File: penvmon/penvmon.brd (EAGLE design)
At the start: 160 x 100 mm, 20 parts, among them IC2 7805TV, U1 ZC563900

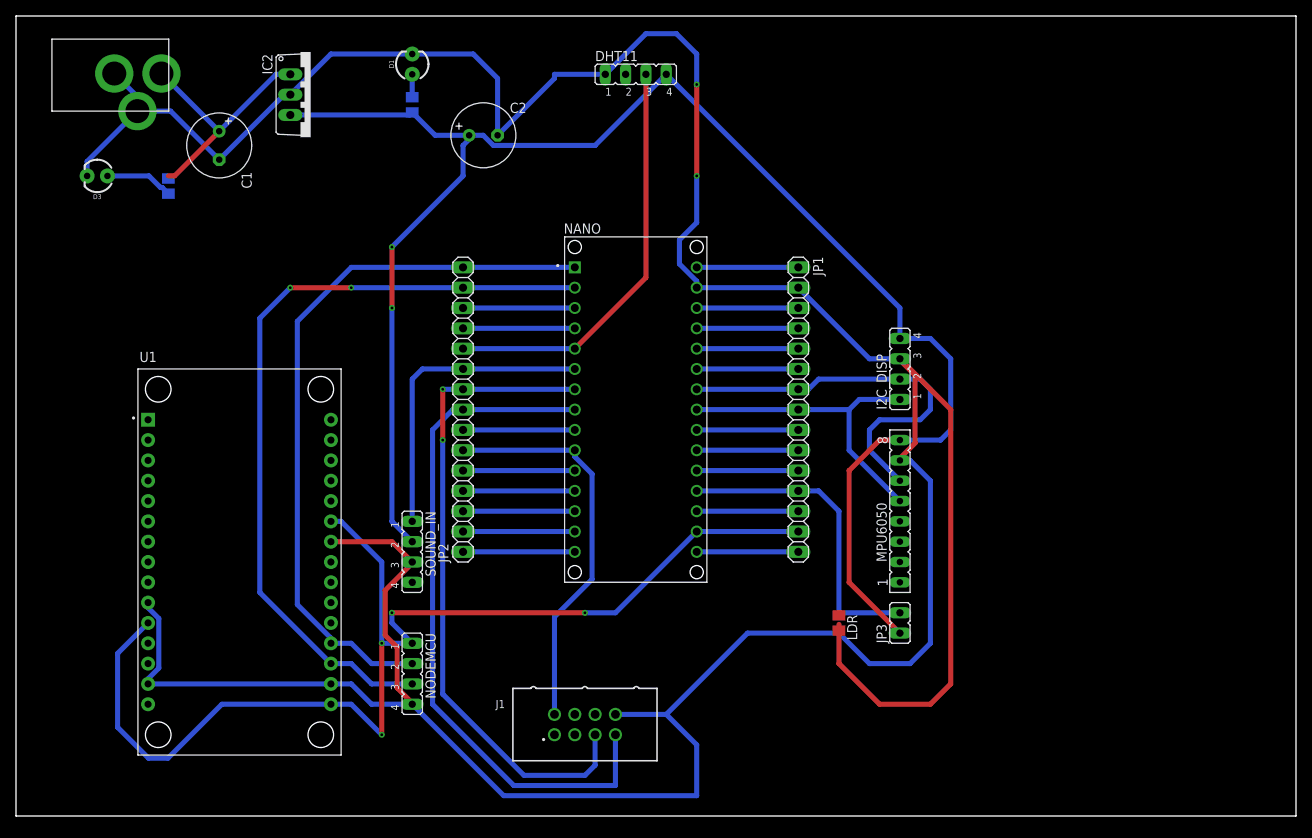
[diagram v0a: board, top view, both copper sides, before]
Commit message: changed Placement- routing and check needed
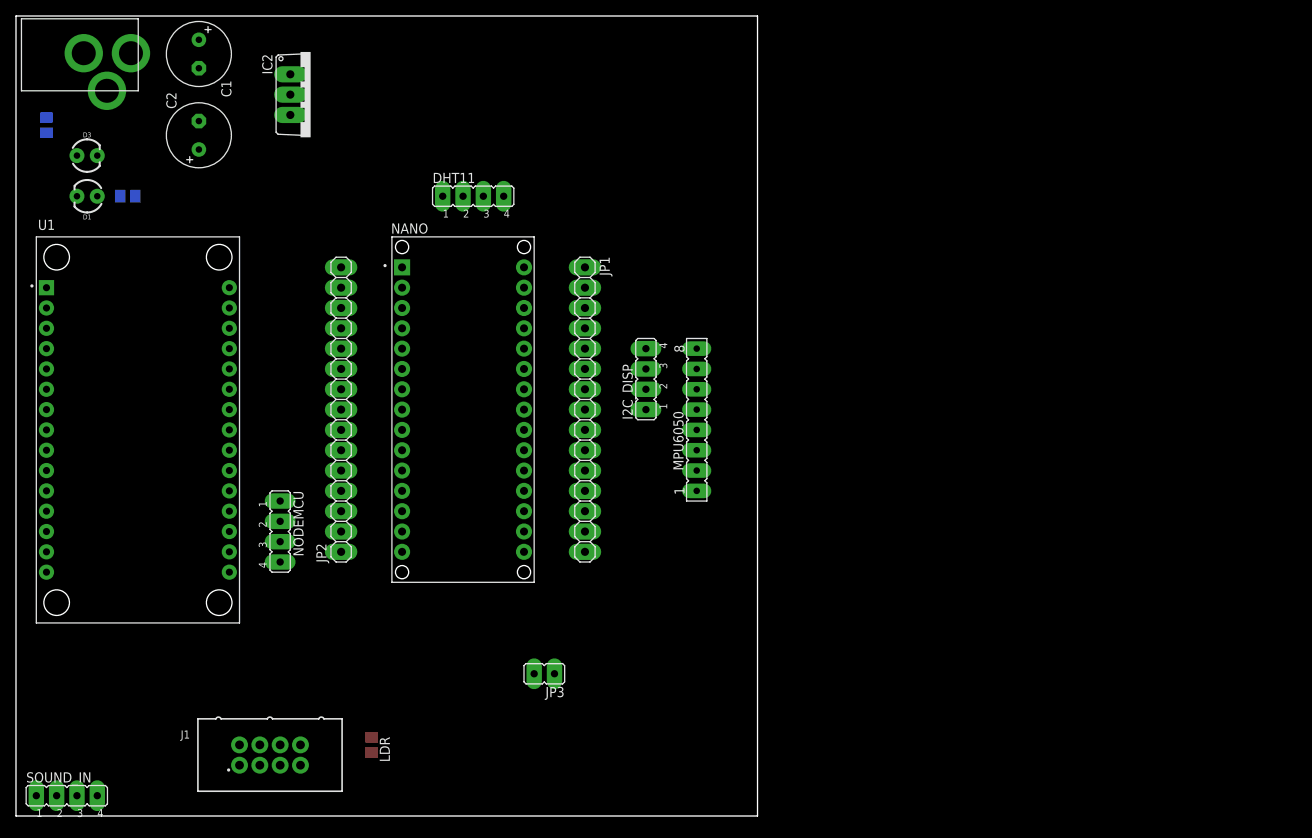
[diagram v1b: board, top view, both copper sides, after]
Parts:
- moved LDR 60.4 mm to (44.5, 8.89)
- moved SOUND_IN 52.9 mm to (6.35, 2.54), turned to 0 degrees
- moved JP3 44.9 mm to (66.0, 17.8), turned to 90 degrees
- moved D1 43.9 mm to (8.89, 77.5), turned to 180 degrees
- moved J1 39.6 mm to (31.8, 7.62)
- moved R1 37.4 mm to (14.0, 77.5), turned to 0 degrees
- moved C2 35.6 mm to (22.9, 85.1), turned to 90 degrees
- moved I2C_DISP 31.8 mm to (78.7, 54.6)
- moved MPU6050 27.9 mm to (85.1, 49.5)
- moved JP1 26.7 mm to (71.1, 50.8)
- moved DHT11 25.4 mm to (57.1, 77.5)
- moved NODEMCU 24.3 mm to (33.0, 35.6)
- moved NANO 21.6 mm to (55.9, 50.8)
- moved U1 20.8 mm to (15.2, 48.3)
- moved R11 17.0 mm to (3.81, 86.4)
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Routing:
- net GND: track 449.7 -> 0.00 mm, vias 2 -> 0
- net 5V: track 207.7 -> 0.00 mm, vias 2 -> 0
- net 3V3: track 147.3 -> 0.00 mm, vias 4 -> 0
- net RXNANO: track 99.0 -> 0.00 mm, vias 2 -> 0
- net TXNANO: track 90.7 -> 0.00 mm
- net OK: track 86.5 -> 0.00 mm
- net LEFT: track 82.2 -> 0.00 mm, vias 2 -> 0
- net DHT: track 51.9 -> 0.00 mm
- net RIGHT: track 49.8 -> 0.00 mm
- net SCL: track 49.4 -> 0.00 mm
- net SDA: track 40.0 -> 0.00 mm
- net SOUND_D0: track 39.9 -> 0.00 mm
- net LDR_SIG: track 39.2 -> 0.00 mm
- net 9_IN: track 30.7 -> 0.00 mm
- net RESET_1: track 14.0 -> 0.00 mm
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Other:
- board size 160 x 100 mm -> 92.7 x 100 mm

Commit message: vibha_layout_done
kindly check the layout once
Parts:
- removed JP3: (no value), jumper:JP1
- removed LDR: 10k, adafruit:M0805
- moved J1 25.5 mm to (57.3, 7.49)
- moved SOUND_IN 5.63 mm to (9.03, 7.49)
- moved DHT11 2.66 mm to (56.0, 79.9), turned to 180 degrees
- moved NODEMCU 1.42 mm to (32.2, 36.7)
- moved C2 1.42 mm to (24.3, 85.0)
- moved I2C_DISP 1.42 mm to (80.1, 54.5)
- moved MPU6050 1.42 mm to (86.5, 49.4)
- moved C1 1.42 mm to (24.3, 95.1)
- moved IC2 1.42 mm to (38.2, 90.0)
- moved JP1 1.42 mm to (72.5, 50.7)
- moved JP2 1.42 mm to (42.0, 50.7)
- moved NANO 1.42 mm to (57.3, 50.7)
- moved U$3 1.42 mm to (6.49, 95.1)
- moved R11 1.42 mm to (5.22, 86.2)
- moved D1 1.42 mm to (10.3, 77.3)
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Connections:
- removed net DOWN: JP2.7, NANO.9
- removed net LDR_SIG: JP1.12, JP3.2, LDR.1, NANO.19
- new net 12: JP1.12, NANO.19
- net 5V: no longer JP3.1
- net BACK: now also J1.4, JP2.7, NANO.9; no longer J1.6
- net DOWN(NA): now also J1.7; no longer J1.4
- net GND: no longer LDR.2
- net OK: now also J1.6; no longer J1.7
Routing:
- net GND: track 0.00 -> 360.2 mm
- net 5V: track 0.00 -> 184.0 mm, vias 0 -> 4
- net 3V3: track 0.00 -> 159.5 mm, vias 0 -> 7
- net SOUND_D0: track 0.00 -> 143.5 mm, vias 0 -> 6
- net LEFT: track 0.00 -> 84.3 mm, vias 0 -> 2
- net OK: track 0.00 -> 54.7 mm
- net BACK: track 0.00 -> 51.1 mm
- net RXNANO: track 0.00 -> 49.8 mm
- net TXNANO: track 0.00 -> 49.8 mm
- net RIGHT: track 0.00 -> 46.8 mm
- net 9_IN: track 0.00 -> 45.6 mm
- net DHT: track 0.00 -> 32.8 mm
- net SDA: track 0.00 -> 21.6 mm
- net SCL: track 0.00 -> 21.6 mm
- net VIN: track 0.00 -> 7.62 mm
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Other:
- board size 92.7 x 100 mm -> 91.9 x 100 mm

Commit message: just_a_little_correction_vibha_project
all the sensors are added and designed
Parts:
- added SOIL_MOI: (no value), jumper:JP4
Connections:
- removed net A7: JP1.5, NANO.26
- new net SOIL_A0: JP1.5, NANO.26, SOIL_MOI.4
- new net SOIL_D0: SOIL_MOI.3
- net 5V: now also SOIL_MOI.1
- net GND: now also SOIL_MOI.2
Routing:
- net GND: track 360.2 -> 407.9 mm
- net SOIL_A0: track 0.00 -> 32.8 mm, vias 0 -> 2
- net 5V: track 184.0 -> 213.4 mm
- net A7: track 7.62 -> 0.00 mm
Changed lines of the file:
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@@
 <attribute name="VALUE" x="89.4207" y="39.243" size="1.27" layer="27" ratio="10" rot="R90"/>
+</element>
+<element name="SOIL_MOI" library="jumper" library_urn="urn:adsk.eagle:library:252" package="JP4" package3d_urn="urn:adsk.eagle:package:15463/1" value="" x="85.2551" y="79.8957" smashed="yes" rot="R270">
+<attribute name="NAME" x="86.9061" y="84.9757" size="1.27" layer="25" ratio="10" rot="R270"/>
+<attribute name="POPULARITY" value="15" x="85.2551" y="79.8957" size="1.778" layer="27" rot="R270" display="off"/>
+<attribute name="VALUE" x="81.1911" y="84.9757" size="1.27" layer="27" ratio="10" rot="R270"/>
 </element>
 </elements>
@@
 <wire x1="47.1297" y1="86.233" x2="57.2897" y2="86.233" width="0.635" layer="16"/>
 <wire x1="72.5297" y1="65.913" x2="75.0697" y2="65.913" width="0.635" layer="16"/>
-<wire x1="75.0697" y1="65.913" x2="76.3397" y2="64.643" width="0.635" layer="16"/>
-<wire x1="76.3397" y1="64.643" x2="76.3397" y2="58.293" width="0.635" layer="16"/>
-<wire x1="76.3397" y1="58.293" x2="78.8797" y2="55.753" width="0.635" layer="16"/>
+<wire x1="75.0697" y1="65.913" x2="77.0636" y2="63.9191" width="0.635" layer="16"/>
+<wire x1="77.0636" y1="63.9191" x2="77.0636" y2="57.5691" width="0.635" layer="16"/>
+<wire x1="77.0636" y1="57.5691" x2="78.8797" y2="55.753" width="0.635" layer="16"/>
 <wire x1="78.8797" y1="55.753" x2="80.1497" y2="55.753" width="0.635" layer="16"/>
 <wire x1="59.8297" y1="67.183" x2="61.0997" y2="65.913" width="0.635" layer="16"/>
@@
 <wire x1="87.8967" y1="55.753" x2="90.043" y2="53.6067" width="0.635" layer="16"/>
 <wire x1="90.043" y1="53.6067" x2="90.043" y2="14.8463" width="0.635" layer="16"/>
-<wire x1="3.5179" y1="43.053" x2="3.0734" y2="43.053" width="0.635" layer="16"/>
 <wire x1="3.0734" y1="43.053" x2="2.47015" y2="42.44975" width="0.635" layer="16"/>
 <wire x1="2.47015" y1="42.44975" x2="1.7907" y2="41.7703" width="0.635" layer="16"/>
 <wire x1="1.7907" y1="43.053" x2="2.2098" y2="43.053" width="0.635" layer="16"/>
 <wire x1="2.2098" y1="43.053" x2="2.921" y2="43.053" width="0.635" layer="16"/>
-<wire x1="3.5179" y1="43.053" x2="4.0386" y2="43.053" width="0.635" layer="16"/>
-<wire x1="4.0386" y1="43.053" x2="5.2197" y2="43.053" width="0.635" layer="16"/>
+<wire x1="3.0734" y1="43.053" x2="5.2197" y2="43.053" width="0.635" layer="16"/>
 <wire x1="2.47015" y1="42.44975" x2="2.2098" y2="42.7101" width="0.635" layer="16"/>
 <wire x1="2.2098" y1="42.7101" x2="2.2098" y2="43.053" width="0.635" layer="16"/>
 <wire x1="3.0734" y1="43.053" x2="2.921" y2="43.053" width="0.635" layer="16"/>
 <wire x1="2.921" y1="43.053" x2="1.7907" y2="44.1833" width="0.635" layer="16"/>
+<contactref element="SOIL_MOI" pad="2"/>
+<wire x1="43.3197" y1="90.043" x2="46.6725" y2="90.043" width="0.635" layer="16"/>
+<wire x1="46.6725" y1="90.043" x2="49.1236" y2="92.4941" width="0.635" layer="16"/>
+<wire x1="49.1236" y1="92.4941" x2="68.6689" y2="92.4941" width="0.635" layer="16"/>
+<wire x1="79.9973" y1="81.1657" x2="85.2551" y2="81.1657" width="0.635" layer="16"/>
+<wire x1="68.6689" y1="92.4941" x2="79.9973" y2="81.1657" width="0.635" layer="16"/>
 </signal>
 <signal name="SCK">
@@
 <contactref element="JP1" pad="6"/>
 <wire x1="64.9097" y1="55.753" x2="72.5297" y2="55.753" width="0.635" layer="16"/>
-</signal>
-<signal name="A7">
-<contactref element="NANO" pad="26"/>
-<contactref element="JP1" pad="5"/>
-<wire x1="64.9097" y1="58.293" x2="72.5297" y2="58.293" width="0.635" layer="16"/>
 </signal>
 <signal name="5V">
@@
 <wire x1="12.8397" y1="35.433" x2="16.6497" y2="39.243" width="0.635" layer="16"/>
 <wire x1="16.6497" y1="39.243" x2="16.6497" y2="77.343" width="0.635" layer="16"/>
+<contactref element="SOIL_MOI" pad="1"/>
+<wire x1="85.2551" y1="83.7057" x2="87.2871" y2="83.7057" width="0.635" layer="16"/>
+<wire x1="89.2937" y1="61.087" x2="86.4997" y2="58.293" width="0.635" layer="16"/>
+<wire x1="87.2871" y1="83.7057" x2="89.2937" y2="81.6991" width="0.635" layer="16"/>
+<wire x1="89.2937" y1="81.6991" x2="89.2937" y2="61.087" width="0.635" layer="16"/>
 </signal>
 <signal name="N$2">
@@
 <contactref element="MPU6050" pad="1"/>
 </signal>
+<signal name="SOIL_D0">
+<contactref element="SOIL_MOI" pad="3"/>
+</signal>
+<signal name="SOIL_A0">
+<contactref element="SOIL_MOI" pad="4"/>
+<contactref element="NANO" pad="26"/>
+<contactref element="JP1" pad="5"/>
+<wire x1="64.9097" y1="58.293" x2="72.5297" y2="58.293" width="0.635" layer="16"/>
+<wire x1="72.5297" y1="58.293" x2="75.5269" y2="58.293" width="0.635" layer="16"/>
+<wire x1="75.5269" y1="58.293" x2="75.6666" y2="58.4327" width="0.635" layer="16"/>
+<via x="75.6666" y="58.4327" extent="1-16" drill="0.35"/>
+<wire x1="75.6666" y1="58.4327" x2="82.6516" y2="65.4177" width="0.635" layer="1"/>
+<wire x1="82.6516" y1="65.4177" x2="83.2739" y2="65.4177" width="0.635" layer="1"/>
+<via x="83.2739" y="65.4177" extent="1-16" drill="0.35"/>
+<wire x1="83.2739" y1="65.4177" x2="83.2739" y2="74.1045" width="0.635" layer="16"/>
+<wire x1="83.2739" y1="74.1045" x2="85.2551" y2="76.0857" width="0.635" layer="16"/>
+</signal>
 </signals>
